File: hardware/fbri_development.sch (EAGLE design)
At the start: 95 parts, among them IC3 TLV70033DCK, J1 AAA_HOLDER, U1 SAM_D20E, U2 SI4060, U3 MAX1947, U4 ANTENOVA_GPS_M10382, U5 S25FS-S, U6 STM32F_48PIN, Y1 8MHz

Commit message: Before trying Direct Tie Tx/Rx
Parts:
- removed J1: AAA_HOLDER, fbri:AAA_HOLDER
- added C19: 4.7µF, resistor:C-EUC0603K
- added C27, C28, C29, C30: 10µF, resistor:C-EUC0603K
- added C31, C32: 100pF, resistor:C-EUC0603K
- added IC1: (no value), SparkFun:V_REG_LM1117SOT223
- added JP16: (no value), SparkFun:M02LOCK
- added R22, R23: 1Ω, microbuilder_v3:RESISTOR_0402
- added U$99: INA216, fbri:INA216
- added U7: LP38501TS-ADJ/NOPB, LP38501TS-ADJ:LP38501TS-ADJ/NOPB
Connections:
- removed net N$1: U6.PA0
- removed net N$5: JP1.2, JP13.1, JP14.1, R5.2, R6.2, U$2.+
- removed net PWR_BR: U6.PB1
- new net 1.2VREG_OUT: C27.1, IC1.OUT, IC1.OUT@1, JP16.2
- new net ADJ_REG_EN: U6.PA3, U7.EN
- new net ADJ_REG_OUT: C29.1, C30.1, C32.1, JP13.2, U7.OUT
- new net ADJ_REG_SWITCHING: U6.PA4, U7.ADJ
- new net I_PA: U$99.OUT
- new net I_STEPUP_IN: U$2.OUT, U6.PA6
- new net I_STEPUP_OUT: U$5.OUT, U6.PB1
- new net I_VDD_GPS: U$62.OUT, U6.PA5
- new net I_VDD_MEM: U$48.OUT, U6.PA2
- new net I_VDD_RADIO: U$60.OUT, U6.PA0
- new net I_VDD_SAMD20: U$30.OUT, U6.PA1
- new net VDD_PA: L2.2, R22.1, R23.1, U$99.-
- new net VDD_STEPUP: JP1.2, JP13.1, JP14.1, JP16.1, R5.2, R6.2, U$2.+, U6.PA7
- net 1.2V: no longer J1.+, JP13.2
- net 1.8V: now also U6.PB0
- net 3.3V: now also JP14.2; no longer U6.PB5
- net 5.0V: now also C19.1, C28.1, C31.1, IC1.IN, U7.IN
- net GND: now also C19.2, C27.2, C28.2, C29.2, C30.2, C31.2, C32.2, IC1.ADJ, U$99.GND, U7.DAP, U7.GND; no longer J1.-
- net RADIO_VDD: now also R22.2, R23.2, U$99.+; no longer L2.2
- net RESETN: now also U1.PA04; no longer U1.PA05, U1.PA14
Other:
- note added: "Busses"
- note added: "USB Interface"
- note removed: "HW v1"
- moved on the sheet: BTN1, C11, C17, C18, C20, C21, C22, C23, C24, C25, C26, C6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

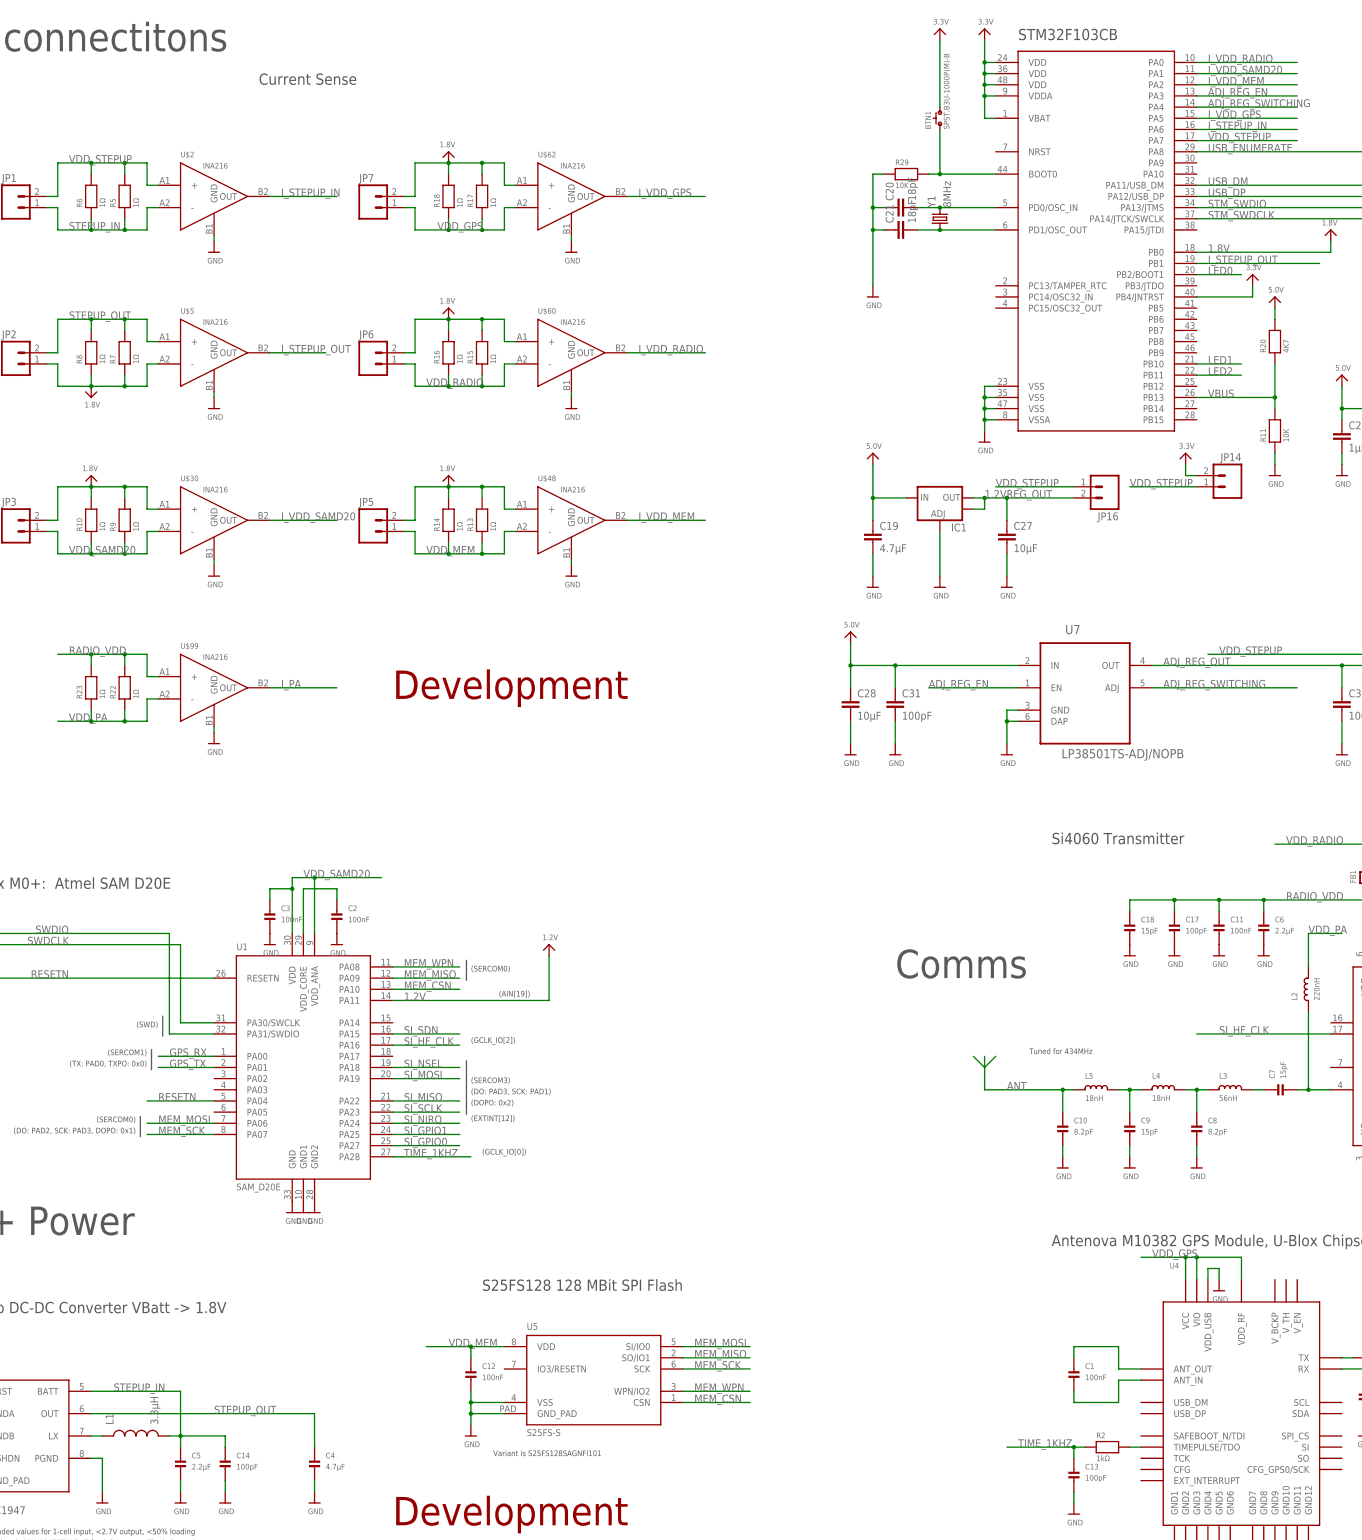
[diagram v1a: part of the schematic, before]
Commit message: Nearly there, about to re-work MAX1947
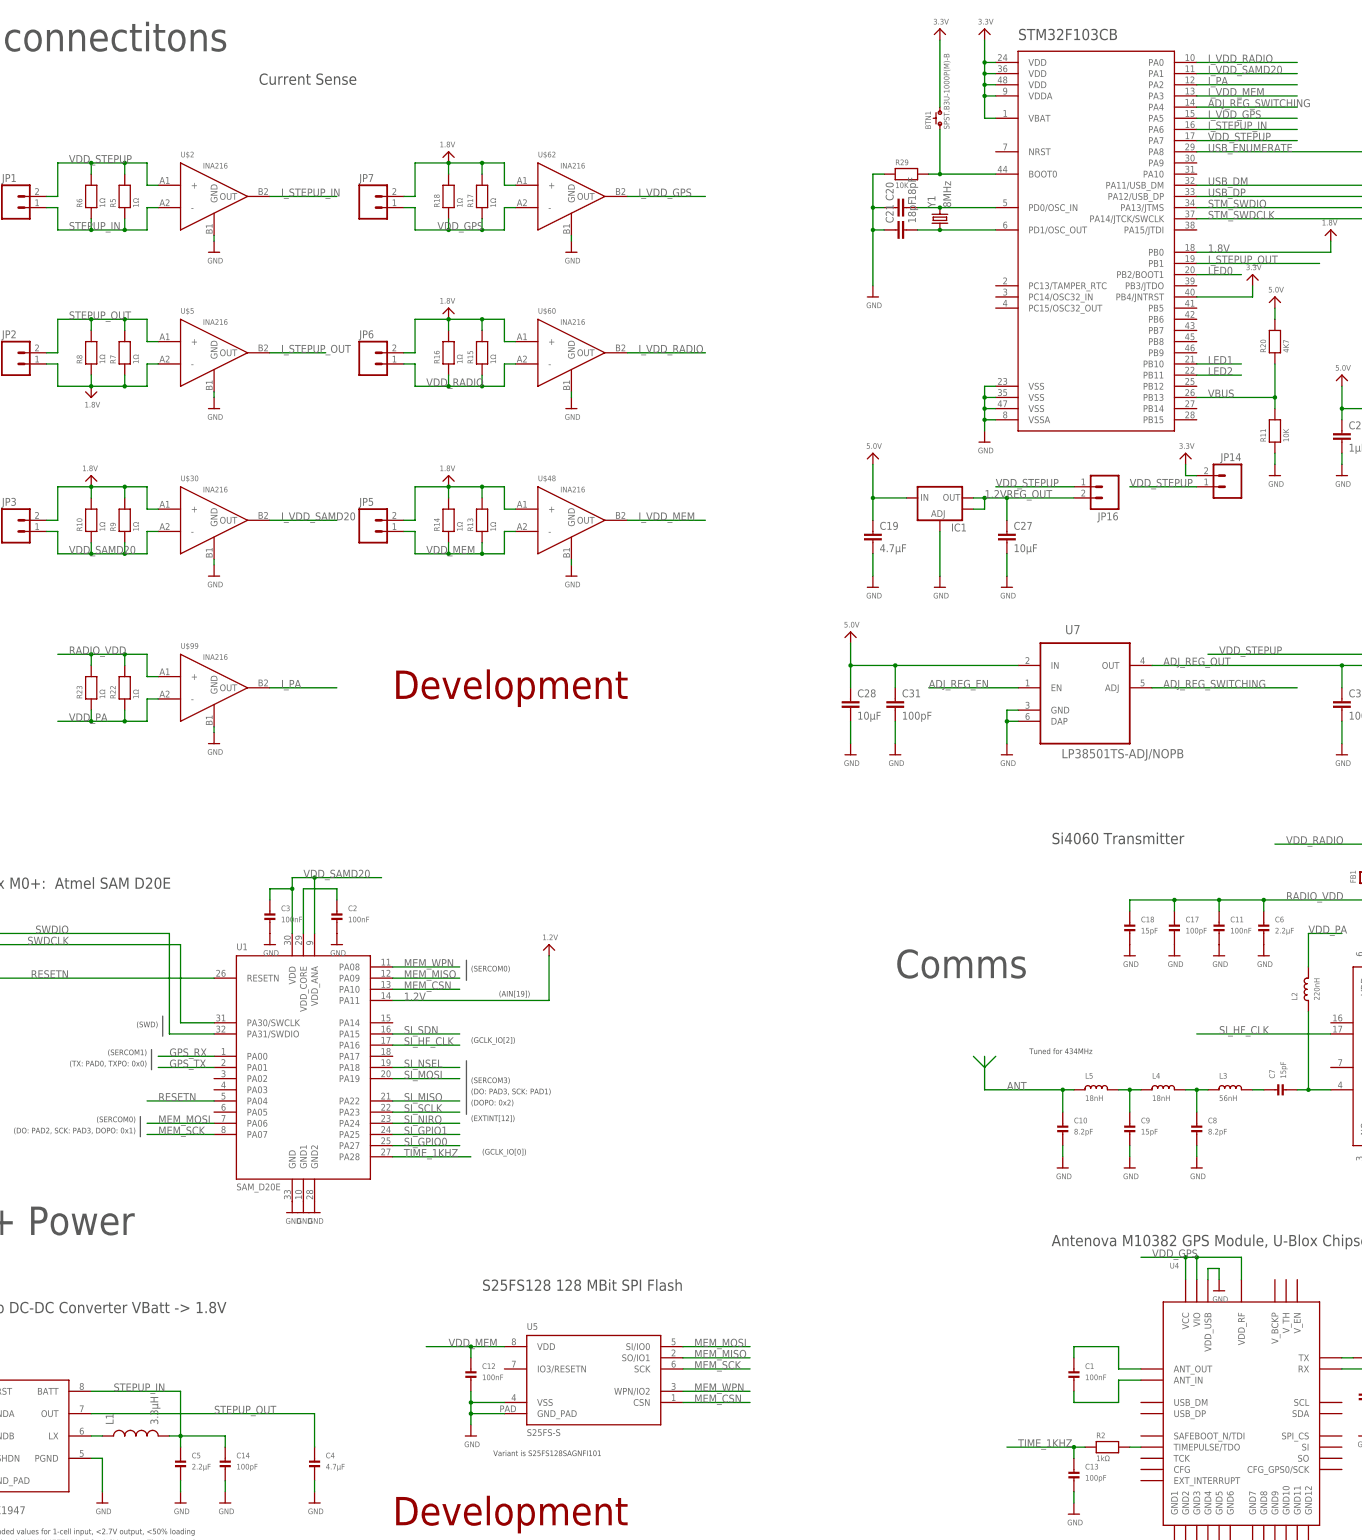
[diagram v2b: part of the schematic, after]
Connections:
- net ADJ_REG_EN: no longer U6.PA3
- net I_PA: now also U6.PA2
- net I_VDD_MEM: now also U6.PA3; no longer U6.PA2
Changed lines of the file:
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@@
 </segment>
 <segment>
-<pinref part="U6" gate="G$1" pin="PA2"/>
-<wire x1="335.28" y1="353.06" x2="358.14" y2="353.06" width="0.1524" layer="91"/>
-<label x="337.82" y="353.06" size="1.778" layer="95"/>
+<pinref part="U6" gate="G$1" pin="PA3"/>
+<wire x1="335.28" y1="350.52" x2="358.14" y2="350.52" width="0.1524" layer="91"/>
+<label x="337.82" y="350.52" size="1.778" layer="95"/>
 </segment>
 </net>
@@
 <label x="274.32" y="215.9" size="1.778" layer="95"/>
 </segment>
-<segment>
-<pinref part="U6" gate="G$1" pin="PA3"/>
-<wire x1="335.28" y1="350.52" x2="358.14" y2="350.52" width="0.1524" layer="91"/>
-<label x="337.82" y="350.52" size="1.778" layer="95"/>
-</segment>
 </net>
 <net name="I_PA" class="0">
@@
 <label x="127" y="215.9" size="1.778" layer="95"/>
 </segment>
+<segment>
+<pinref part="U6" gate="G$1" pin="PA2"/>
+<wire x1="335.28" y1="353.06" x2="358.14" y2="353.06" width="0.1524" layer="91"/>
+<label x="337.82" y="353.06" size="1.778" layer="95"/>
+</segment>
 </net>

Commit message: Before rename
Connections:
- net SI_HF_CLK: now also U1.PA17; no longer U1.PA16
- net SI_SDN: now also U1.PA16; no longer U1.PA15
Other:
- note added: "(GCLK_IO[3])"
- note removed: "(GCLK_IO[2])"
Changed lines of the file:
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@@
 <wire x1="169.164" y1="153.924" x2="169.164" y2="149.352" width="0.1524" layer="97"/>
 <text x="93.98" y="114.554" size="1.27" layer="97" font="vector" ratio="11" rot="MR0">(DO: PAD2, SCK: PAD3, DOPO: 0x1)</text>
-<text x="170.18" y="135.128" size="1.27" layer="97" font="vector" ratio="11">(GCLK_IO[2])</text>
+<text x="170.18" y="132.588" size="1.27" layer="97" font="vector" ratio="11">(GCLK_IO[3])</text>
 <text x="96.52" y="132.334" size="1.27" layer="97" font="vector" ratio="11" rot="MR0">(SERCOM1)</text>
 <wire x1="97.536" y1="133.604" x2="97.536" y2="129.032" width="0.1524" layer="97"/>
@@
 </segment>
 <segment>
-<pinref part="U1" gate="G$1" pin="PA16"/>
-<wire x1="152.4" y1="134.62" x2="167.64" y2="134.62" width="0.1524" layer="91"/>
-<label x="154.94" y="134.62" size="1.778" layer="95" ratio="11"/>
-</segment>
-<segment>
 <wire x1="17.78" y1="256.54" x2="33.02" y2="256.54" width="0.1524" layer="91"/>
 <label x="20.32" y="256.54" size="1.778" layer="95"/>
 <pinref part="JP10" gate="G$1" pin="2"/>
 </segment>
+<segment>
+<pinref part="U1" gate="G$1" pin="PA17"/>
+<wire x1="152.4" y1="132.08" x2="167.64" y2="132.08" width="0.1524" layer="91"/>
+<label x="154.94" y="132.08" size="1.778" layer="95"/>
+</segment>
 </net>
 <net name="SI_SDN" class="0">
-<segment>
-<pinref part="U1" gate="G$1" pin="PA15"/>
-<wire x1="152.4" y1="137.16" x2="167.64" y2="137.16" width="0.1524" layer="91"/>
-<label x="154.94" y="137.16" size="1.778" layer="95" ratio="11"/>
-</segment>
 <segment>
 <pinref part="U2" gate="G$1" pin="SDN"/>
@@
 <label x="20.32" y="281.94" size="1.778" layer="95"/>
 </segment>
-</net>
+<segment>
+<pinref part="U1" gate="G$1" pin="PA16"/>
+<wire x1="152.4" y1="134.62" x2="167.64" y2="134.62" width="0.1524" layer="91"/>
+<label x="154.94" y="134.62" size="1.778" layer="95"/>
+</segment>
+</net>
